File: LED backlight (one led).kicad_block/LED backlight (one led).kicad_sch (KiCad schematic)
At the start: 2 parts

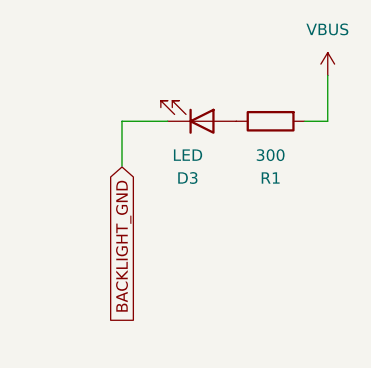
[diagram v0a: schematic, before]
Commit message: resstor footprint (I think!) and the net label for leds
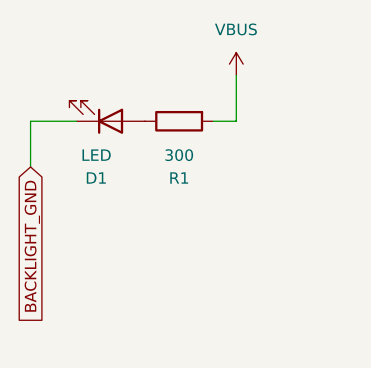
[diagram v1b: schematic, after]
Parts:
- R1: footprint (none) -> Resistor_THT:R_Axial_DIN0207_L6.3mm_D2.5mm_P10.16mm_Horizontal
- renumbered D3 to D1
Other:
- moved on the sheet: D1, R1
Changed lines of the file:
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@@
 	(wire
 		(pts
-			(xy 299.72 90.17) (xy 297.18 90.17)
-		)
-		(stroke
-			(width 0)
-			(type default)
-		)
-	)
-	(wire
-		(pts
-			(xy 276.86 90.17) (xy 281.94 90.17)
-		)
-		(stroke
-			(width 0)
-			(type default)
-		)
-	)
-	(wire
-		(pts
-			(xy 299.72 85.09) (xy 299.72 90.17)
-		)
-		(stroke
-			(width 0)
-			(type default)
-		)
-	)
-	(wire
-		(pts
-			(xy 276.86 90.17) (xy 276.86 95.25)
+			(xy 289.56 90.17) (xy 287.02 90.17)
+		)
+		(stroke
+			(width 0)
+			(type default)
+		)
+	)
+	(wire
+		(pts
+			(xy 266.7 90.17) (xy 266.7 95.25)
+		)
+		(stroke
+			(width 0)
+			(type default)
+		)
+	)
+	(wire
+		(pts
+			(xy 266.7 90.17) (xy 271.78 90.17)
+		)
+		(stroke
+			(width 0)
+			(type default)
+		)
+	)
+	(wire
+		(pts
+			(xy 289.56 85.09) (xy 289.56 90.17)
 		)
 		(stroke
@@
 	(global_label "BACKLIGHT_GND"
 		(shape input)
-		(at 276.86 95.25 270)
+		(at 266.7 95.25 270)
 		(fields_autoplaced yes)
 		(effects
@@
 		)
 		(property "Intersheetrefs" "${INTERSHEET_REFS}"
-			(at 276.86 113.1729 90)
+			(at 266.7 113.1729 90)
 			(hide yes)
 			(show_name no)
@@
 	(symbol
 		(lib_id "power:VBUS")
-		(at 299.72 85.09 0)
+		(at 289.56 85.09 0)
 		(unit 1)
 		(body_style 1)
@@
 		(fields_autoplaced yes)
 		(property "Reference" "#PWR011"
-			(at 299.72 88.9 0)
+			(at 289.56 88.9 0)
 			(hide yes)
 			(show_name no)
@@
 		)
 		(property "Value" "VBUS"
-			(at 299.72 80.01 0)
+			(at 289.56 80.01 0)
 			(show_name no)
 			(do_not_autoplace no)
@@
 		)
 		(property "Footprint" ""
-			(at 299.72 85.09 0)
+			(at 289.56 85.09 0)
 			(hide yes)
 			(show_name no)
@@
 		)
 		(property "Datasheet" ""
-			(at 299.72 85.09 0)
+			(at 289.56 85.09 0)
 			(hide yes)
 			(show_name no)
@@
 		)
 		(property "Description" "Power symbol creates a global label with name \"VBUS\""
-			(at 299.72 85.09 0)
+			(at 289.56 85.09 0)
 			(hide yes)
 			(show_name no)
@@
 	(symbol
 		(lib_id "Device:R")
-		(at 293.37 90.17 90)
+		(at 283.21 90.17 90)
 		(mirror x)
 		(unit 1)
@@
 		(dnp no)
 		(property "Reference" "R1"
-			(at 293.37 96.52 90)
+			(at 283.21 96.52 90)
 			(show_name no)
 			(do_not_autoplace no)
@@
 		)
 		(property "Value" "300"
-			(at 293.37 93.98 90)
-			(show_name no)
-			(do_not_autoplace no)
-			(effects
-				(font
-					(size 1.27 1.27)
-				)
-			)
-		)
-		(property "Footprint" ""
-			(at 293.37 88.392 90)
+			(at 283.21 93.98 90)
+			(show_name no)
+			(do_not_autoplace no)
+			(effects
+				(font
+					(size 1.27 1.27)
+				)
+			)
+		)
+		(property "Footprint" "Resistor_THT:R_Axial_DIN0207_L6.3mm_D2.5mm_P10.16mm_Horizontal"
+			(at 283.21 88.392 90)
 			(hide yes)
 			(show_name no)
@@
 		)
 		(property "Datasheet" ""
-			(at 293.37 90.17 0)
+			(at 283.21 90.17 0)
 			(hide yes)
 			(show_name no)
@@
 		)
 		(property "Description" "Resistor"
-			(at 293.37 90.17 0)
+			(at 283.21 90.17 0)
 			(hide yes)
 			(show_name no)
@@
 	(symbol
 		(lib_id "Device:LED")
-		(at 285.75 90.17 0)
+		(at 275.59 90.17 0)
 		(mirror x)
 		(unit 1)
@@
 		(in_pos_files yes)
 		(dnp no)
-		(property "Reference" "D3"
-			(at 284.1625 96.52 0)
+		(property "Reference" "D1"
+			(at 274.0025 96.52 0)
 			(show_name no)
 			(do_not_autoplace no)
@@
 		)
 		(property "Value" "LED"
-			(at 284.1625 93.98 0)
+			(at 274.0025 93.98 0)
 			(show_name no)
 			(do_not_autoplace no)
@@
 		)
 		(property "Footprint" "LED_THT:LED_D5.0mm"
-			(at 285.75 90.17 0)
+			(at 275.59 90.17 0)
 			(hide yes)
 			(show_name no)
@@
 		)
 		(property "Datasheet" ""
-			(at 285.75 90.17 0)
+			(at 275.59 90.17 0)
 			(hide yes)
 			(show_name no)
@@
 		)
 		(property "Description" "Light emitting diode"
-			(at 285.75 90.17 0)
+			(at 275.59 90.17 0)
 			(hide yes)
 			(show_name no)
@@
 		)
 		(property "Sim.Pins" "1=K 2=A"
-			(at 285.75 90.17 0)
+			(at 275.59 90.17 0)
 			(hide yes)
 			(show_name no)
@@
 			(project "kicad-mobiflight-device-blocks-worksheet"
 				(path "/4714e232-3dfb-45f4-a0c3-3539b78f5138"
-					(reference "D3")
+					(reference "D1")
 					(unit 1)
 				)
